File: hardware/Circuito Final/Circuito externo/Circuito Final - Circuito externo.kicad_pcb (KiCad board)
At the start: 2 copper layers, 124.6 x 134.4 mm, 82 parts, among them J1 Conn_02x19_Odd_Even, J2 Conn_02x19_Odd_Even, J3 Conn_01x02, J4 Conn_01x02, J5 Conn_01x03_Pin, Q1 FDMS6681Z, Q2 FDMS6681Z, Q3 MMBT2222A, SW1 SW_SPDT, SW2 SW_DIP_x04, SW3 SW_DIP_x04, SW4 SW_DIP_x01, SW5 SW_DIP_x01, SW6 SW_DIP_x01, U1 Opamp_Quad, U2 ICL7660, U3 INA180A1, U4 INA180A1

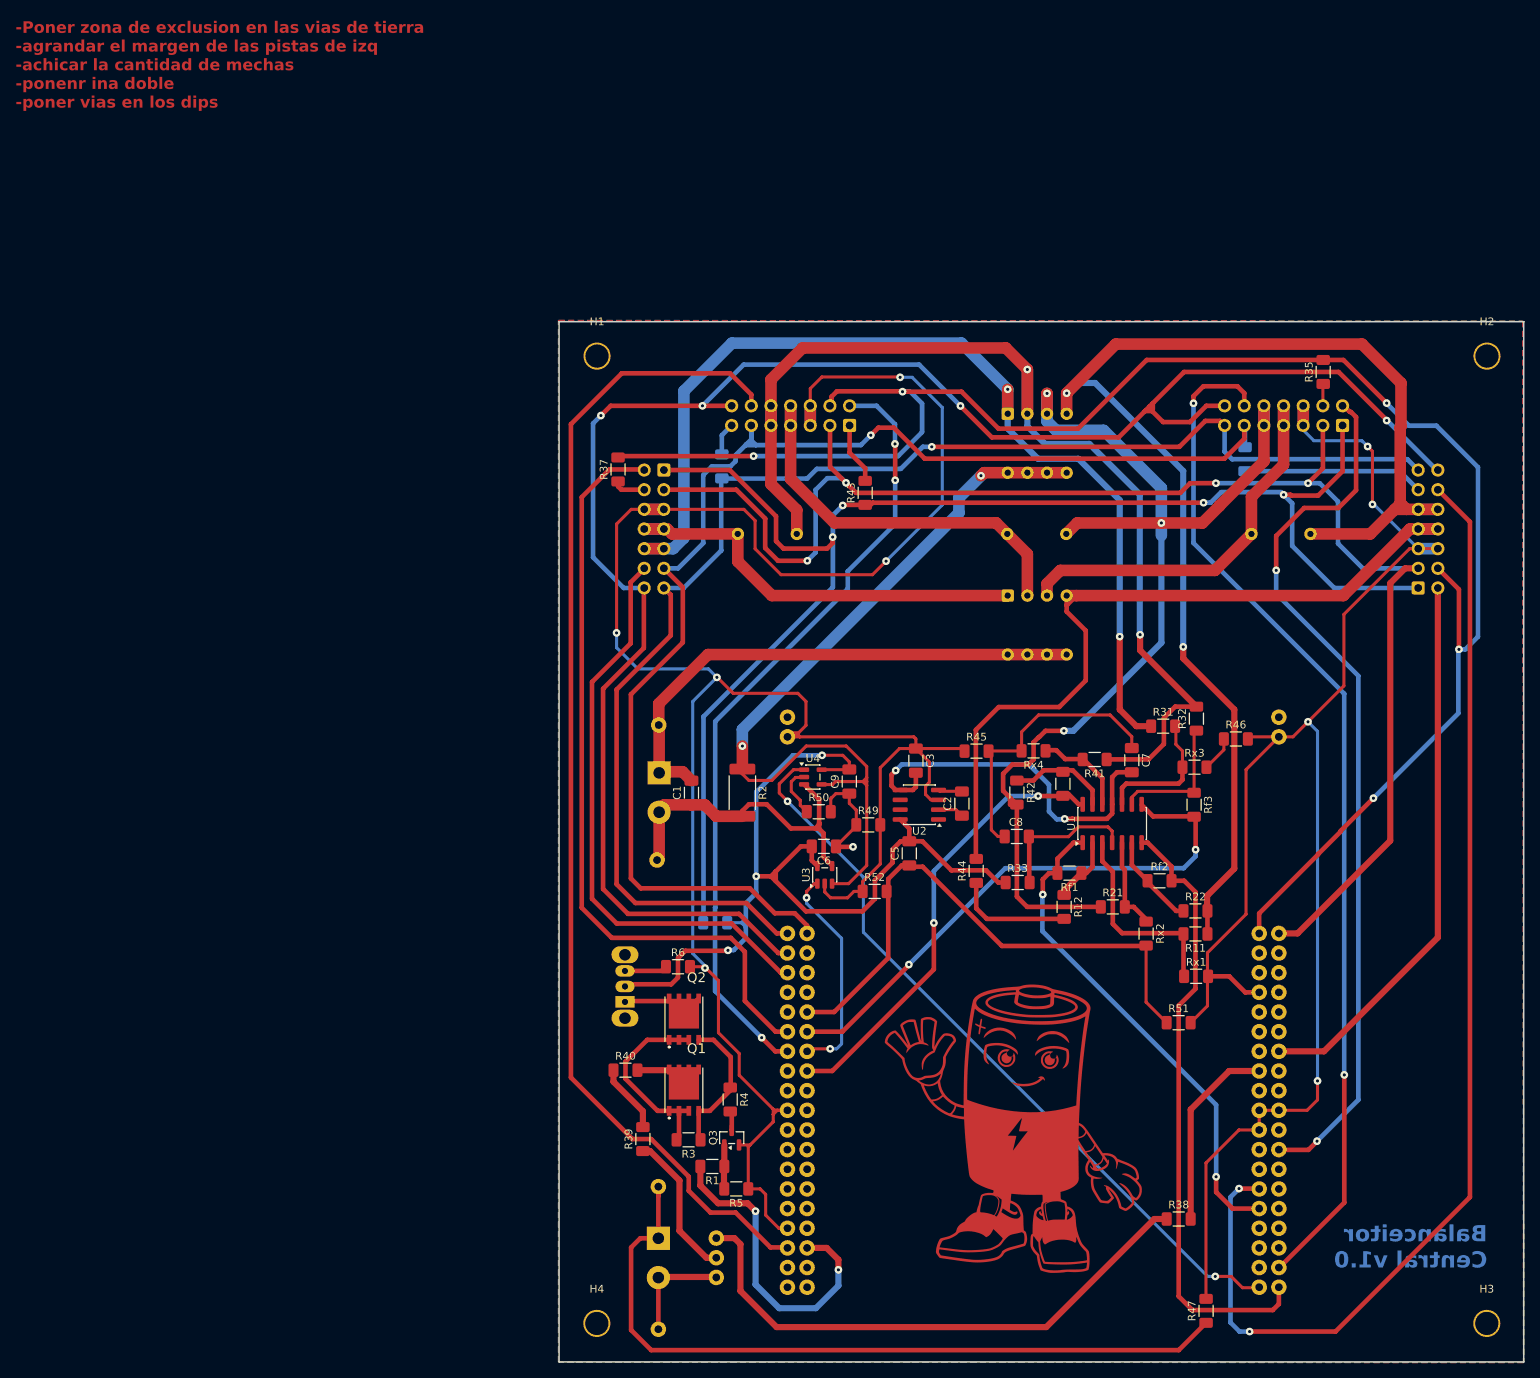
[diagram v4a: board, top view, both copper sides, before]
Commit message: agranda los pads de las vias a 1.7mm
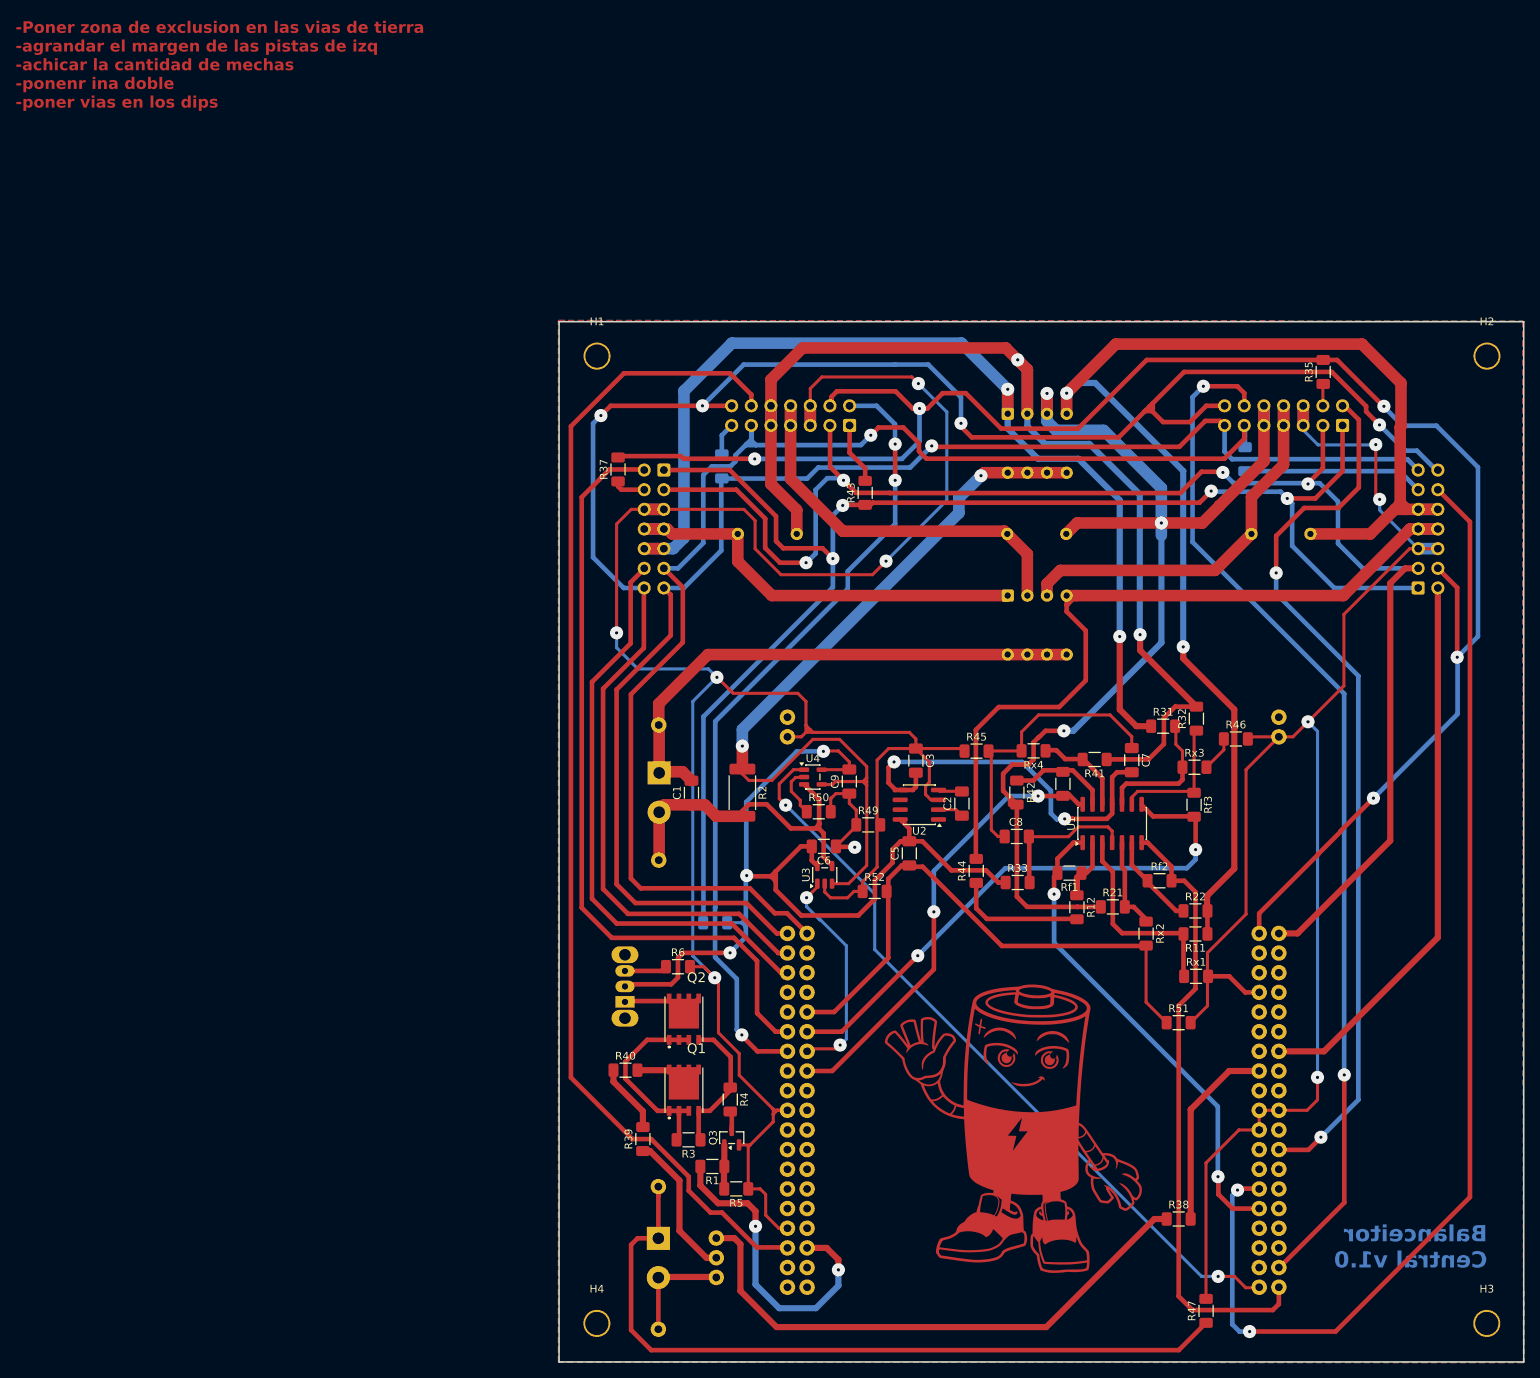
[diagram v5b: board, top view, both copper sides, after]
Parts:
- moved R12 1.65 mm to (105.0, 115.8)
- moved TP1 0.23 mm to (50.9, 109.8)
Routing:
- net GND: track 736.8 -> 740.0 mm
- net /Bit_0: track 235.9 -> 238.5 mm
- net /Vcc_out: track 313.9 -> 315.9 mm
- net /banco1_med: track 64.4 -> 62.5 mm
- net /bus_pos_3: track 138.0 -> 139.7 mm
- net /bus_neg_1: track 116.5 -> 118.2 mm
- net /Data_3: track 102.3 -> 103.7 mm
- net /clock: track 195.0 -> 196.2 mm
- net /Vcc_neg: track 48.1 -> 49.1 mm
- net /latch: track 234.5 -> 233.5 mm
- net /bus_pos_salida: track 108.7 -> 109.4 mm
- net Net-(U1A--): track 8.64 -> 8.00 mm
